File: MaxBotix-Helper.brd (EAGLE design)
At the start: 19.7 x 14.2 mm, 4 parts

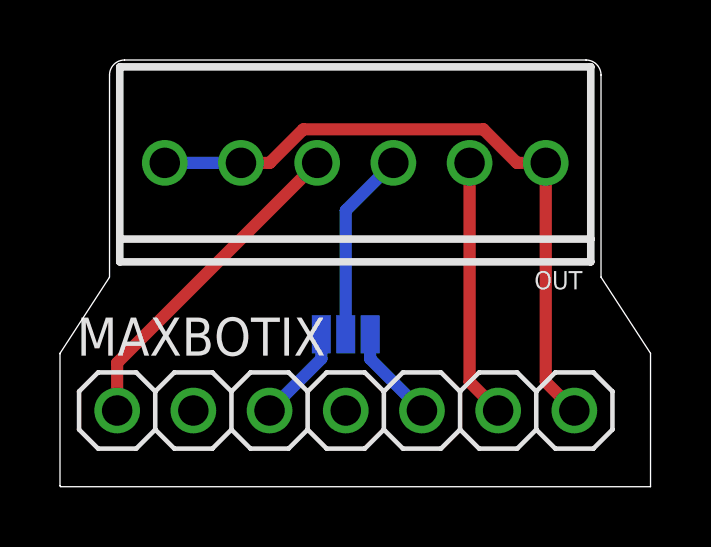
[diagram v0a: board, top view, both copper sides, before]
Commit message: Move signal select etc. to not be behind MB board
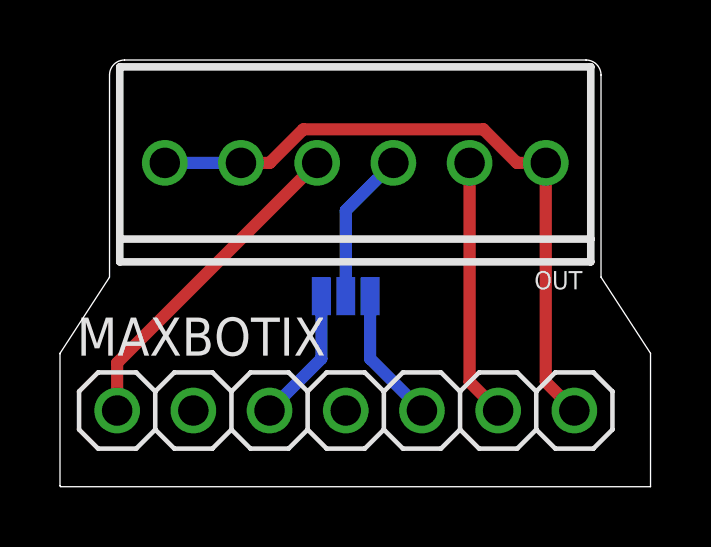
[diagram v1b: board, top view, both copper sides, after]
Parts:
- moved JP1 1.27 mm to (9.53, 6.35)
- moved LOGO1 0.46 mm to (16.3, 5.59), turned to 180 degrees
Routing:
- net SERIAL: track 3.26 -> 4.53 mm
- net SIGNAL: track 6.37 -> 5.10 mm
- net V_ANALOG: track 3.26 -> 4.53 mm
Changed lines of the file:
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@@
 <layer number="22" name="bPlace" color="7" fill="1" visible="no" active="yes"/>
 <layer number="23" name="tOrigins" color="15" fill="1" visible="yes" active="yes"/>
-<layer number="24" name="bOrigins" color="15" fill="1" visible="no" active="yes"/>
+<layer number="24" name="bOrigins" color="15" fill="1" visible="yes" active="yes"/>
 <layer number="25" name="tNames" color="7" fill="1" visible="no" active="yes"/>
 <layer number="26" name="bNames" color="7" fill="1" visible="no" active="yes"/>
@@
 <text x="9.144" y="9.652" size="1.016" layer="52" font="vector" ratio="15" rot="MR270">TC</text>
 <text x="6.604" y="9.652" size="1.016" layer="52" font="vector" ratio="15" rot="MR270">GND</text>
-<text x="8.128" y="4.826" size="0.6604" layer="52" font="vector" ratio="15" rot="MR0">Analog</text>
-<text x="10.922" y="5.461" size="0.6604" layer="52" font="vector" ratio="15" rot="MR180">Serial</text>
-<text x="12.065" y="5.842" size="0.6604" layer="52" font="vector" ratio="15" rot="MR0">Signal select</text>
+<text x="8.128" y="6.096" size="0.6604" layer="52" font="vector" ratio="15" rot="MR0">Analog</text>
+<text x="10.922" y="6.731" size="0.6604" layer="52" font="vector" ratio="15" rot="MR180">Serial</text>
+<text x="11.938" y="4.953" size="0.6604" layer="52" font="vector" ratio="15" rot="MR0">Signal select</text>
 <wire x1="18.034" y1="6.985" x2="19.685" y2="4.445" width="0" layer="20"/>
 <wire x1="19.685" y1="4.445" x2="19.685" y2="0" width="0" layer="20"/>
-<text x="4.064" y="13.208" size="1.016" layer="52" font="vector" ratio="15" rot="MR180">T corr.</text>
+<text x="3.937" y="13.208" size="1.016" layer="52" font="vector" ratio="15" rot="MR180">T corr.</text>
 <wire x1="8.636" y1="11.938" x2="8.636" y2="12.7" width="0.1524" layer="52"/>
-<wire x1="8.636" y1="12.7" x2="8.128" y2="12.7" width="0.1524" layer="52"/>
-<wire x1="3.937" y1="12.7" x2="3.429" y2="12.7" width="0.1524" layer="52"/>
+<wire x1="8.636" y1="12.7" x2="8.382" y2="12.7" width="0.1524" layer="52"/>
+<wire x1="3.683" y1="12.7" x2="3.429" y2="12.7" width="0.1524" layer="52"/>
 <wire x1="3.429" y1="12.7" x2="3.429" y2="11.938" width="0.1524" layer="52"/>
 <text x="11.43" y="13.208" size="1.016" layer="52" font="vector" ratio="15" rot="MR180">Logger</text>
@@
 <text x="4.445" y="4.445" size="1.016" layer="51" font="vector" ratio="15" rot="R90" align="center-left">PW</text>
 <text x="1.905" y="4.445" size="1.016" layer="51" font="vector" ratio="15" rot="R90" align="center-left">TC</text>
-<text x="9.8425" y="0.635" size="0.6096" layer="51" align="center">MaxBotix-Helper v0.0 - A. Wickert - 2019.03.21</text>
-<text x="4.1275" y="4.445" size="0.508" layer="52" rot="MR0">Northern
+<text x="9.8425" y="0.635" size="0.5842" layer="51" font="vector" align="center">MaxBotix-Helper v0.0 - A. Wickert - 2019.03.21</text>
+<text x="4.699" y="5.461" size="0.508" layer="52" font="vector" rot="MR0">Northern
 Widget LLC</text>
 </plain>
@@
 </autorouter>
 <elements>
-<element name="JP1" library="SparkFun-Jumpers" library_urn="urn:adsk.eagle:library:528" package="SMT-JUMPER_3_1-NC_PASTE_NO-SILK" package3d_urn="urn:adsk.eagle:package:39291/1" value="JUMPER-SMT_3_1-NC_PASTE_NO-SILK" x="9.525" y="5.08" rot="MR180">
-<attribute name="NAME" x="9.525" y="3.937" size="0.6096" layer="26" font="vector" ratio="20" rot="MR180" align="bottom-center"/>
-<attribute name="VALUE" x="9.525" y="6.223" size="0.6096" layer="28" font="vector" ratio="20" rot="MR180" align="top-center"/>
+<element name="JP1" library="SparkFun-Jumpers" library_urn="urn:adsk.eagle:library:528" package="SMT-JUMPER_3_1-NC_PASTE_NO-SILK" package3d_urn="urn:adsk.eagle:package:39291/1" value="JUMPER-SMT_3_1-NC_PASTE_NO-SILK" x="9.525" y="6.35" rot="MR180">
+<attribute name="NAME" x="9.525" y="5.207" size="0.6096" layer="26" font="vector" ratio="20" rot="MR180" align="bottom-center"/>
+<attribute name="VALUE" x="9.525" y="7.493" size="0.6096" layer="28" font="vector" ratio="20" rot="MR180" align="top-center"/>
 </element>
-<element name="LOGO1" library="bschulz" package="OSHW-LOGO-S" package3d_urn="urn:adsk.eagle:package:37099/1" value="OSHW-LOGOS" x="16.51" y="5.207" rot="MR0"/>
+<element name="LOGO1" library="bschulz" package="OSHW-LOGO-S" package3d_urn="urn:adsk.eagle:package:37099/1" value="OSHW-LOGOS" x="16.256" y="5.588" rot="MR180"/>
 <element name="MAXBOTIX" library="bschulz" package="1X07" value="" x="9.525" y="2.54">
 <attribute name="NAME" x="0.5588" y="4.3688" size="1.27" layer="25" ratio="10"/>
@@
 <contactref element="JP1" pad="1"/>
 <wire x1="6.985" y1="2.54" x2="8.7122" y2="4.2672" width="0.4064" layer="16"/>
-<wire x1="8.7122" y1="4.2672" x2="8.7122" y2="5.08" width="0.4064" layer="16"/>
+<wire x1="8.7122" y1="6.35" x2="8.7122" y2="4.2672" width="0.4064" layer="16"/>
 </signal>
 <signal name="SERIAL">
 <contactref element="MAXBOTIX" pad="5"/>
 <contactref element="JP1" pad="3"/>
-<wire x1="10.3378" y1="5.08" x2="10.3378" y2="4.2672" width="0.4064" layer="16"/>
+<wire x1="10.3378" y1="6.35" x2="10.3378" y2="4.2672" width="0.4064" layer="16"/>
 <wire x1="10.3378" y1="4.2672" x2="12.065" y2="2.54" width="0.4064" layer="16"/>
 </signal>
@@
 <contactref element="JP1" pad="2"/>
 <wire x1="11.1125" y1="10.795" x2="9.525" y2="9.2075" width="0.4064" layer="16"/>
-<wire x1="9.525" y1="9.2075" x2="9.525" y2="5.08" width="0.4064" layer="16"/>
+<wire x1="9.525" y1="9.2075" x2="9.525" y2="6.35" width="0.4064" layer="16"/>
 </signal>
 </signals>

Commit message: Aesthetics
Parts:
- moved LOGO1 1.09 mm to (15.4, 4.95), turned to 0 degrees
- moved JP1 0.63 mm to (9.53, 5.71)
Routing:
- net SERIAL: track 4.53 -> 3.89 mm
- net SIGNAL: track 5.10 -> 5.74 mm
- net V_ANALOG: track 4.53 -> 3.89 mm
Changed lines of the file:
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@@
 <text x="9.144" y="9.652" size="1.016" layer="52" font="vector" ratio="15" rot="MR270">TC</text>
 <text x="6.604" y="9.652" size="1.016" layer="52" font="vector" ratio="15" rot="MR270">GND</text>
-<text x="8.128" y="6.096" size="0.6604" layer="52" font="vector" ratio="15" rot="MR0">Analog</text>
-<text x="10.922" y="6.731" size="0.6604" layer="52" font="vector" ratio="15" rot="MR180">Serial</text>
-<text x="11.938" y="4.953" size="0.6604" layer="52" font="vector" ratio="15" rot="MR0">Signal select</text>
+<text x="8.128" y="5.461" size="0.6604" layer="52" font="vector" ratio="15" rot="MR0">Analog</text>
+<text x="10.922" y="6.096" size="0.6604" layer="52" font="vector" ratio="15" rot="MR180">Serial</text>
+<text x="11.938" y="4.318" size="0.6604" layer="52" font="vector" ratio="15" rot="MR0">Signal select</text>
 <wire x1="18.034" y1="6.985" x2="19.685" y2="4.445" width="0" layer="20"/>
 <wire x1="19.685" y1="4.445" x2="19.685" y2="0" width="0" layer="20"/>
@@
 <text x="1.905" y="4.445" size="1.016" layer="51" font="vector" ratio="15" rot="R90" align="center-left">TC</text>
 <text x="9.8425" y="0.635" size="0.5842" layer="51" font="vector" align="center">MaxBotix-Helper v0.0 - A. Wickert - 2019.03.21</text>
-<text x="4.699" y="5.461" size="0.508" layer="52" font="vector" rot="MR0">Northern
+<text x="4.191" y="4.445" size="0.508" layer="52" font="vector" rot="MR0">Northern
 Widget LLC</text>
 </plain>
@@
 </autorouter>
 <elements>
-<element name="JP1" library="SparkFun-Jumpers" library_urn="urn:adsk.eagle:library:528" package="SMT-JUMPER_3_1-NC_PASTE_NO-SILK" package3d_urn="urn:adsk.eagle:package:39291/1" value="JUMPER-SMT_3_1-NC_PASTE_NO-SILK" x="9.525" y="6.35" rot="MR180">
-<attribute name="NAME" x="9.525" y="5.207" size="0.6096" layer="26" font="vector" ratio="20" rot="MR180" align="bottom-center"/>
-<attribute name="VALUE" x="9.525" y="7.493" size="0.6096" layer="28" font="vector" ratio="20" rot="MR180" align="top-center"/>
+<element name="JP1" library="SparkFun-Jumpers" library_urn="urn:adsk.eagle:library:528" package="SMT-JUMPER_3_1-NC_PASTE_NO-SILK" package3d_urn="urn:adsk.eagle:package:39291/1" value="JUMPER-SMT_3_1-NC_PASTE_NO-SILK" x="9.525" y="5.715" rot="MR180">
+<attribute name="NAME" x="9.525" y="4.572" size="0.6096" layer="26" font="vector" ratio="20" rot="MR180" align="bottom-center"/>
+<attribute name="VALUE" x="9.525" y="6.858" size="0.6096" layer="28" font="vector" ratio="20" rot="MR180" align="top-center"/>
 </element>
-<element name="LOGO1" library="bschulz" package="OSHW-LOGO-S" package3d_urn="urn:adsk.eagle:package:37099/1" value="OSHW-LOGOS" x="16.256" y="5.588" rot="MR180"/>
+<element name="LOGO1" library="bschulz" package="OSHW-LOGO-S" package3d_urn="urn:adsk.eagle:package:37099/1" value="OSHW-LOGOS" x="15.367" y="4.953" rot="MR0"/>
 <element name="MAXBOTIX" library="bschulz" package="1X07" value="" x="9.525" y="2.54">
 <attribute name="NAME" x="0.5588" y="4.3688" size="1.27" layer="25" ratio="10"/>
@@
 <contactref element="JP1" pad="1"/>
 <wire x1="6.985" y1="2.54" x2="8.7122" y2="4.2672" width="0.4064" layer="16"/>
-<wire x1="8.7122" y1="6.35" x2="8.7122" y2="4.2672" width="0.4064" layer="16"/>
+<wire x1="8.7122" y1="5.715" x2="8.7122" y2="4.2672" width="0.4064" layer="16"/>
 </signal>
 <signal name="SERIAL">
 <contactref element="MAXBOTIX" pad="5"/>
 <contactref element="JP1" pad="3"/>
-<wire x1="10.3378" y1="6.35" x2="10.3378" y2="4.2672" width="0.4064" layer="16"/>
+<wire x1="10.3378" y1="5.715" x2="10.3378" y2="4.2672" width="0.4064" layer="16"/>
 <wire x1="10.3378" y1="4.2672" x2="12.065" y2="2.54" width="0.4064" layer="16"/>
 </signal>
@@
 <contactref element="JP1" pad="2"/>
 <wire x1="11.1125" y1="10.795" x2="9.525" y2="9.2075" width="0.4064" layer="16"/>
-<wire x1="9.525" y1="9.2075" x2="9.525" y2="6.35" width="0.4064" layer="16"/>
+<wire x1="9.525" y1="9.2075" x2="9.525" y2="5.715" width="0.4064" layer="16"/>
 </signal>
 </signals>
